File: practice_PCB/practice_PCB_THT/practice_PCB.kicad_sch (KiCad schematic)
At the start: 14 parts, among them J1 5V, J2 GND

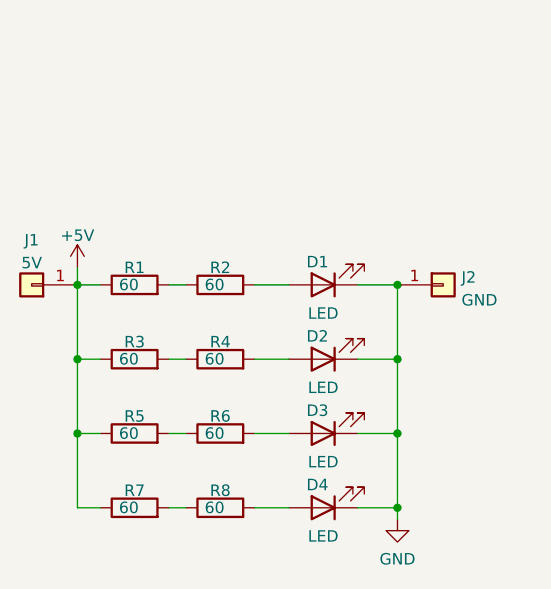
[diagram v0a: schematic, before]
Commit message: change page layout and export a pdf file
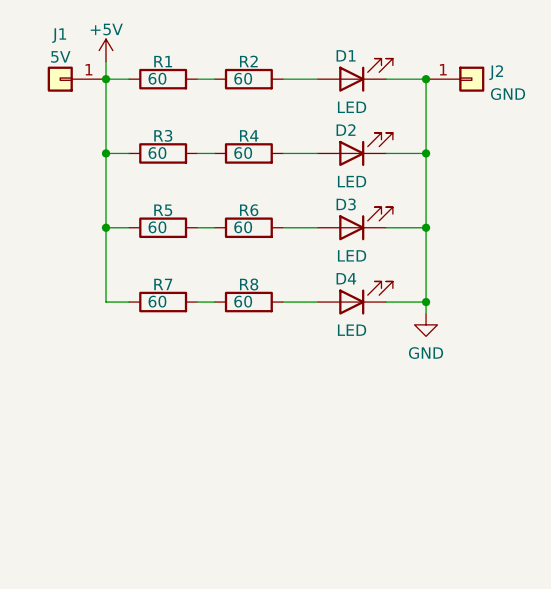
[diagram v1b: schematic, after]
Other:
- company: (none) -> Netz39 e.V.
- title: (none) -> Übungs-Lötset-THT
- moved on the sheet: D1, D2, D3, D4, J1, J2, R1, R2, R3, R4, R5, R6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
